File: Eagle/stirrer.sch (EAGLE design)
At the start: 13 parts, among them IC1 7805, Q1 2N3904

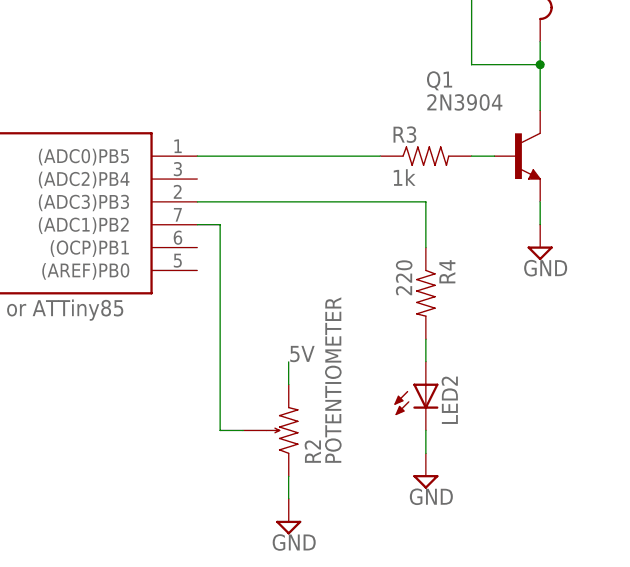
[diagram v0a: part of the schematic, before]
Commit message: Changing R4 from 220 to 1k.
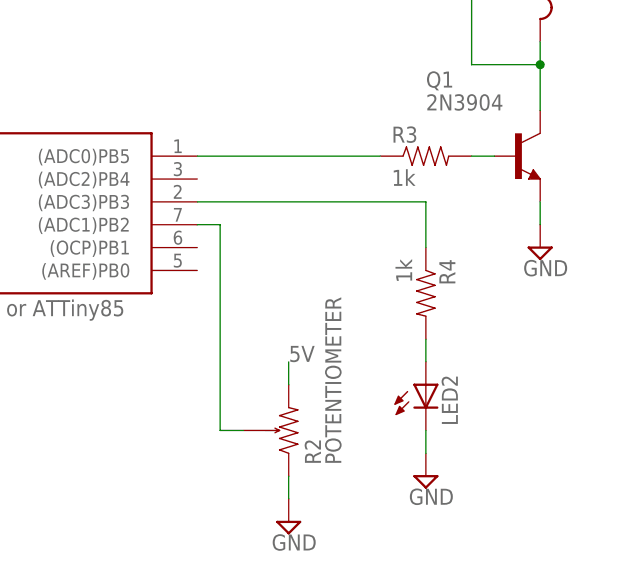
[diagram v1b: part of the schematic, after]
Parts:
- R4: value 220 -> 1k
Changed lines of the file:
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@@
 <part name="SUPPLY8" library="supply2" deviceset="GND" device=""/>
 <part name="R3" library="SparkFun-Passives" deviceset="RESISTOR" device="PTH-1/4W" value="1k"/>
-<part name="R4" library="SparkFun-Passives" deviceset="RESISTOR" device="PTH-1/4W" value="220"/>
+<part name="R4" library="SparkFun-Passives" deviceset="RESISTOR" device="PTH-1/4W" value="1k"/>
 <part name="LED2" library="adafruit" deviceset="LED" device="5MM"/>
 <part name="SUPPLY9" library="supply2" deviceset="GND" device=""/>
